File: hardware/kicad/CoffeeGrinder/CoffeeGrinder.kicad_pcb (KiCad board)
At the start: 2 copper layers, 92.5 x 65 mm, 15 parts, among them U1 ESP32-DevKitC

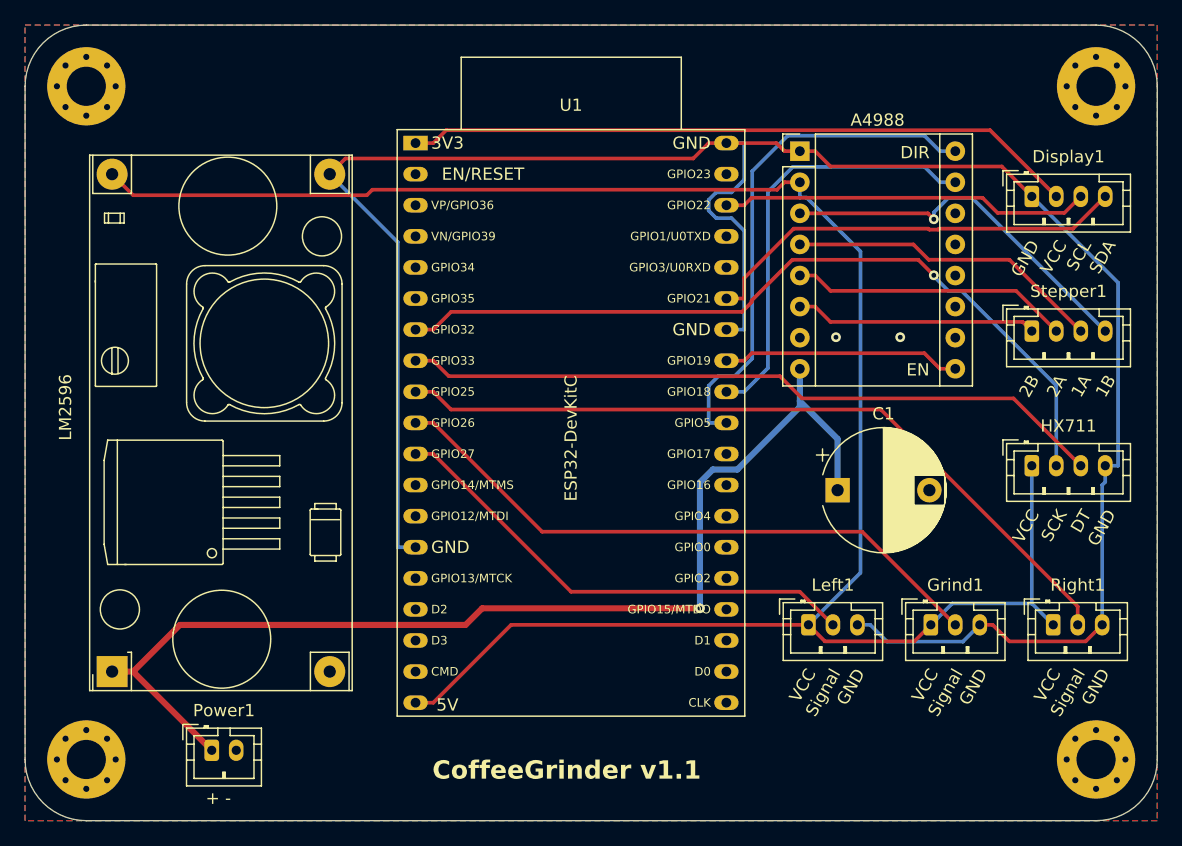
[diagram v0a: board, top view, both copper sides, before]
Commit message: Replace stepper motor with 5010 brushless motor 360KV
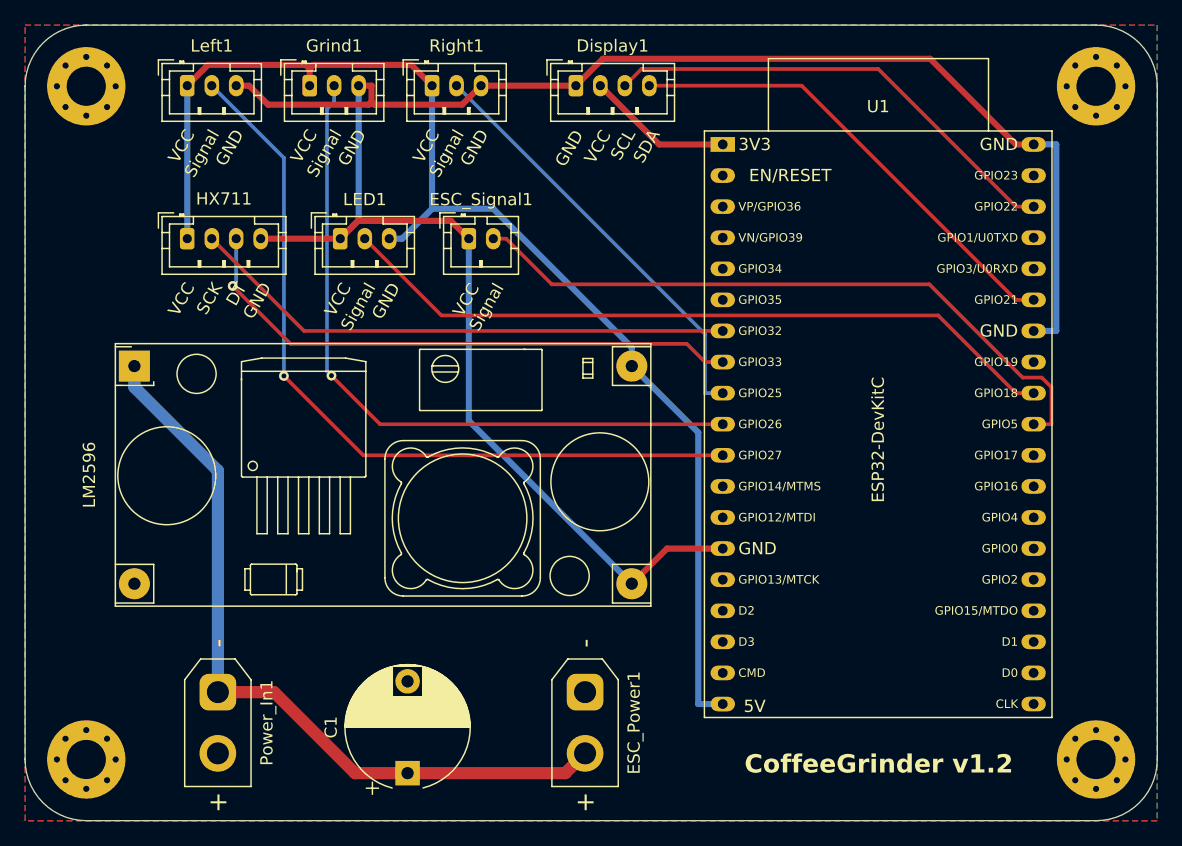
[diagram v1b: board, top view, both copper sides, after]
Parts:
- removed A4988: Pololu_Breakout_A4988, Module:Pololu_Breakout-16_15.2x20.3mm
- removed Power1: Conn_01x02_Pin, Connector_JST:JST_PH_B2B-PH-K_1x02_P2.00mm_Vertical
- removed Stepper1: Conn_01x04_Pin, Connector_JST:JST_PH_B4B-PH-K_1x04_P2.00mm_Vertical
- added ESC_Power1: Conn_01x02, Connector_AMASS:AMASS_XT30UPB-F_1x02_P5.0mm_Vertical, F.Cu at (120.8, 104.5)
- added ESC_Signal1: Conn_01x02_Pin, Connector_JST:JST_PH_B2B-PH-K_1x02_P2.00mm_Vertical, F.Cu at (111.2, 67.5)
- added LED1: Conn_01x03_Pin, Connector_JST:JST_PH_B3B-PH-K_1x03_P2.00mm_Vertical, F.Cu at (100.8, 67.5)
- added Power_In1: Conn_01x02_Pin, Connector_AMASS:AMASS_XT30UPB-M_1x02_P5.0mm_Vertical, F.Cu at (90.8, 104.5)
- moved HX711 71.5 mm to (88.2, 67.5)
- moved Grind1 67.2 mm to (98.2, 55.0)
- moved Left1 67.2 mm to (88.2, 55.0)
- moved Right1 67.2 mm to (108.2, 55.0)
- moved C1 42.1 mm to (106.2, 111.1), turned to 90 degrees
- moved Display1 38.3 mm to (120.0, 55.0)
- moved U1 25.1 mm to (132.0, 59.8)
- moved LM2596 25.0 mm to (83.9, 77.9), turned to 0 degrees
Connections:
- U1 pad 31: Net-(A4988-~{ENABLE}) -> unconnected-(U1-GPIO19-Pad31)
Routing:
- net Net-(Grind1-Pin_1): track 166.2 -> 104.5 mm
- net Net-(Display1-VCC): track 55.0 -> 12.0 mm
- net Net-(A4988-1B): track 30.7 -> 0.00 mm, vias 1 -> 0
- net +24V: track 91.9 -> 62.9 mm, vias 1 -> 0
- net Net-(Right1-Pin_2): track 62.9 -> 35.0 mm
- net Net-(A4988-1A): track 25.9 -> 0.00 mm
- net Net-(Left1-Pin_2): track 39.9 -> 64.7 mm, vias 0 -> 1
- net Net-(LED1-Pin_2): track 35.3 -> 59.9 mm
- net Net-(A4988-2A): track 22.8 -> 0.00 mm
- net Net-(HX711-Pin_2): track 65.6 -> 44.9 mm, vias 1 -> 0
- net Net-(A4988-2B): track 19.8 -> 0.00 mm
- net Net-(A4988-~{ENABLE}): track 19.5 -> 0.00 mm
- net Net-(ESC_Signal1-Pin_2): track 42.6 -> 55.1 mm
- net Net-(Display1-GND): track 177.8 -> 165.4 mm
- net Net-(HX711-Pin_3): track 57.9 -> 46.6 mm, vias 0 -> 1
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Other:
- board text added: "CoffeeGrinder v1.2"
- board text removed: "+ -"
- board text removed: "1A"
- board text removed: "1B"
- board text removed: "2A"
- board text removed: "2B"
- board text removed: "CoffeeGrinder v1.1"
- board text removed: "DIR"
- board text removed: "EN"
